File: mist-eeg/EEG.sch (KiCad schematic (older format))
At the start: 62 parts, among them J4 Electrodes, U11 ADS1299

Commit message: Hooked-up the SoM
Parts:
- renumbered TP10 to TP11
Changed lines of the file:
@@
 	1800 1500 1750 1500
 $Comp
-L power:GND #PWR089
+L power:GND #PWR088
 U 1 1 60A911F0
 P 1900 1600
-F 0 "#PWR089" H 1900 1350 50  0001 C CNN
+F 0 "#PWR088" H 1900 1350 50  0001 C CNN
 F 1 "GND" V 1905 1472 50  0000 R CNN
 F 2 "" H 1900 1600 50  0001 C CNN
@@
 	2100 3450 2200 3450
 $Comp
-L power:GND #PWR091
+L power:GND #PWR090
 U 1 1 60AB1BC7
 P 2100 3700
-F 0 "#PWR091" H 2100 3450 50  0001 C CNN
+F 0 "#PWR090" H 2100 3450 50  0001 C CNN
 F 1 "GND" H 2105 3527 50  0000 C CNN
 F 2 "" H 2100 3700 50  0001 C CNN
@@
 	9650 1400 9650 1350
 $Comp
-L Connector:TestPoint TP10
+L Connector:TestPoint TP11
 U 1 1 60AC454D
 P 9350 1200
-F 0 "TP10" H 9293 1318 50  0000 R CNN
+F 0 "TP11" H 9293 1318 50  0000 R CNN
 F 1 "VREFP" H 9293 1227 50  0000 R CNN
 F 2 "TestPoint:TestPoint_Pad_D1.0mm" H 9550 1200 50  0001 C CNN
@@
 	2000 6250 1950 6250
 $Comp
-L power:GND #PWR094
+L power:GND #PWR093
 U 1 1 60ACA9A2
 P 2300 6300
-F 0 "#PWR094" H 2300 6050 50  0001 C CNN
+F 0 "#PWR093" H 2300 6050 50  0001 C CNN
 F 1 "GND" V 2305 6172 50  0000 R CNN
 F 2 "" H 2300 6300 50  0001 C CNN
@@
 	2250 6250 2250 6150
 $Comp
-L power:GND #PWR085
+L power:GND #PWR084
 U 1 1 60AD4C0C
 P 1000 6700
-F 0 "#PWR085" H 1000 6450 50  0001 C CNN
+F 0 "#PWR084" H 1000 6450 50  0001 C CNN
 F 1 "GND" V 1005 6572 50  0000 R CNN
 F 2 "" H 1000 6700 50  0001 C CNN
@@
 	1000 6550 1050 6550
 $Comp
-L power:GND #PWR084
+L power:GND #PWR083
 U 1 1 60ADFB3C
 P 1000 6250
-F 0 "#PWR084" H 1000 6000 50  0001 C CNN
+F 0 "#PWR083" H 1000 6000 50  0001 C CNN
 F 1 "GND" V 1005 6122 50  0000 R CNN
 F 2 "" H 1000 6250 50  0001 C CNN
@@
 MOSI
 $Comp
-L power:GND #PWR087
+L power:GND #PWR086
 U 1 1 611E3BD9
 P 1350 4350
-F 0 "#PWR087" H 1350 4100 50  0001 C CNN
+F 0 "#PWR086" H 1350 4100 50  0001 C CNN
 F 1 "GND" H 1355 4177 50  0000 C CNN
 F 2 "" H 1350 4350 50  0001 C CNN
@@
 $EndComp
 $Comp
-L power:GND #PWR083
+L power:GND #PWR082
 U 1 1 611E3D9B
 P 850 2050
-F 0 "#PWR083" H 850 1800 50  0001 C CNN
+F 0 "#PWR082" H 850 1800 50  0001 C CNN
 F 1 "GND" H 855 1877 50  0000 C CNN
 F 2 "" H 850 2050 50  0001 C CNN
@@
 $EndComp
 $Comp
-L power:GND #PWR092
+L power:GND #PWR091
 U 1 1 611E4134
 P 2250 2450
-F 0 "#PWR092" H 2250 2200 50  0001 C CNN
+F 0 "#PWR091" H 2250 2200 50  0001 C CNN
 F 1 "GND" H 2255 2277 50  0000 C CNN
 F 2 "" H 2250 2450 50  0001 C CNN
@@
 $EndComp
 $Comp
-L power:GND #PWR0100
+L power:GND #PWR099
 U 1 1 611E45D1
 P 5950 5200
-F 0 "#PWR0100" H 5950 4950 50  0001 C CNN
+F 0 "#PWR099" H 5950 4950 50  0001 C CNN
 F 1 "GND" H 5955 5027 50  0000 C CNN
 F 2 "" H 5950 5200 50  0001 C CNN
@@
 $EndComp
 $Comp
-L power:GND #PWR0104
+L power:GND #PWR0103
 U 1 1 611E8589
 P 7700 5200
-F 0 "#PWR0104" H 7700 4950 50  0001 C CNN
+F 0 "#PWR0103" H 7700 4950 50  0001 C CNN
 F 1 "GND" H 7705 5027 50  0000 C CNN
 F 2 "" H 7700 5200 50  0001 C CNN
@@
 $EndComp
 $Comp
-L power:GND #PWR0103
+L power:GND #PWR0102
 U 1 1 611E895E
 P 7700 4200
-F 0 "#PWR0103" H 7700 3950 50  0001 C CNN
+F 0 "#PWR0102" H 7700 3950 50  0001 C CNN
 F 1 "GND" H 7705 4027 50  0000 C CNN
 F 2 "" H 7700 4200 50  0001 C CNN
@@
 $EndComp
 $Comp
-L power:GND #PWR0102
+L power:GND #PWR0101
 U 1 1 611E8B6C
 P 7700 3200
-F 0 "#PWR0102" H 7700 2950 50  0001 C CNN
+F 0 "#PWR0101" H 7700 2950 50  0001 C CNN
 F 1 "GND" H 7705 3027 50  0000 C CNN
 F 2 "" H 7700 3200 50  0001 C CNN
@@
 $EndComp
 $Comp
-L power:GND #PWR0101
+L power:GND #PWR0100
 U 1 1 611E8DAA
 P 7700 2150
-F 0 "#PWR0101" H 7700 1900 50  0001 C CNN
+F 0 "#PWR0100" H 7700 1900 50  0001 C CNN
 F 1 "GND" H 7705 1977 50  0000 C CNN
 F 2 "" H 7700 2150 50  0001 C CNN
@@
 $EndComp
 $Comp
-L power:GND #PWR097
+L power:GND #PWR096
 U 1 1 611E8FCE
 P 5950 2150
-F 0 "#PWR097" H 5950 1900 50  0001 C CNN
+F 0 "#PWR096" H 5950 1900 50  0001 C CNN
 F 1 "GND" H 5955 1977 50  0000 C CNN
 F 2 "" H 5950 2150 50  0001 C CNN
@@
 $EndComp
 $Comp
-L power:GND #PWR098
+L power:GND #PWR097
 U 1 1 611E9362
 P 5950 3200
-F 0 "#PWR098" H 5950 2950 50  0001 C CNN
+F 0 "#PWR097" H 5950 2950 50  0001 C CNN
 F 1 "GND" H 5955 3027 50  0000 C CNN
 F 2 "" H 5950 3200 50  0001 C CNN
@@
 $EndComp
 $Comp
-L power:GND #PWR099
+L power:GND #PWR098
 U 1 1 611E959E
 P 5950 4200
-F 0 "#PWR099" H 5950 3950 50  0001 C CNN
+F 0 "#PWR098" H 5950 3950 50  0001 C CNN
 F 1 "GND" H 5955 4027 50  0000 C CNN
 F 2 "" H 5950 4200 50  0001 C CNN
@@
 $EndComp
 $Comp
-L power:GND #PWR0106
+L power:GND #PWR0105
 U 1 1 611EC7A4
 P 9750 1450
-F 0 "#PWR0106" H 9750 1200 50  0001 C CNN
+F 0 "#PWR0105" H 9750 1200 50  0001 C CNN
 F 1 "GND" H 9755 1277 50  0000 C CNN
 F 2 "" H 9750 1450 50  0001 C CNN
@@
 $EndComp
 $Comp
-L power:GND #PWR0107
+L power:GND #PWR0106
 U 1 1 611EFAB9
 P 9900 6250
-F 0 "#PWR0107" H 9900 6000 50  0001 C CNN
+F 0 "#PWR0106" H 9900 6000 50  0001 C CNN
 F 1 "GND" H 9905 6077 50  0000 C CNN
 F 2 "" H 9900 6250 50  0001 C CNN
@@
 $EndComp
 $Comp
-L power:GND #PWR096
+L power:GND #PWR095
 U 1 1 611EFD90
 P 3950 5500
-F 0 "#PWR096" H 3950 5250 50  0001 C CNN
+F 0 "#PWR095" H 3950 5250 50  0001 C CNN
 F 1 "GND" H 3955 5327 50  0000 C CNN
 F 2 "" H 3950 5500 50  0001 C CNN
@@
 $EndComp
 $Comp
-L power:GND #PWR095
+L power:GND #PWR094
 U 1 1 611F02B8
 P 3950 4200
-F 0 "#PWR095" H 3950 3950 50  0001 C CNN
+F 0 "#PWR094" H 3950 3950 50  0001 C CNN
 F 1 "GND" H 3955 4027 50  0000 C CNN
 F 2 "" H 3950 4200 50  0001 C CNN
@@
 $EndComp
 $Comp
-L power:GND #PWR0105
+L power:GND #PWR0104
 U 1 1 611F35AF
 P 9350 4600
-F 0 "#PWR0105" H 9350 4350 50  0001 C CNN
+F 0 "#PWR0104" H 9350 4350 50  0001 C CNN
 F 1 "GND" H 9355 4427 50  0000 C CNN
 F 2 "" H 9350 4600 50  0001 C CNN
@@
 	1350 2700 1350 2800
 $Comp
-L power:GND #PWR086
+L power:GND #PWR085
 U 1 1 60DCA2D0
 P 1350 3050
-F 0 "#PWR086" H 1350 2800 50  0001 C CNN
+F 0 "#PWR085" H 1350 2800 50  0001 C CNN
 F 1 "GND" H 1355 2877 50  0000 C CNN
 F 2 "" H 1350 3050 50  0001 C CNN
@@
 Connection ~ 1350 3000
 $Comp
-L power:+3V3 #PWR088
+L power:+3V3 #PWR087
 U 1 1 6110D1DA
 P 1800 1450
-F 0 "#PWR088" H 1800 1300 50  0001 C CNN
+F 0 "#PWR087" H 1800 1300 50  0001 C CNN
 F 1 "+3V3" H 1815 1623 50  0000 C CNN
 F 2 "" H 1800 1450 50  0001 C CNN
@@
 $EndComp
 $Comp
-L power:+3V3 #PWR090
+L power:+3V3 #PWR089
 U 1 1 6110DA17
 P 2100 3350
-F 0 "#PWR090" H 2100 3200 50  0001 C CNN
+F 0 "#PWR089" H 2100 3200 50  0001 C CNN
 F 1 "+3V3" H 2115 3523 50  0000 C CNN
 F 2 "" H 2100 3350 50  0001 C CNN
@@
 $EndComp
 $Comp
-L power:+3V3 #PWR093
+L power:+3V3 #PWR092
 U 1 1 6110E217
 P 2250 6900
-F 0 "#PWR093" H 2250 6750 50  0001 C CNN
+F 0 "#PWR092" H 2250 6750 50  0001 C CNN
 F 1 "+3V3" V 2265 7028 50  0000 L CNN
 F 2 "" H 2250 6900 50  0001 C CNN

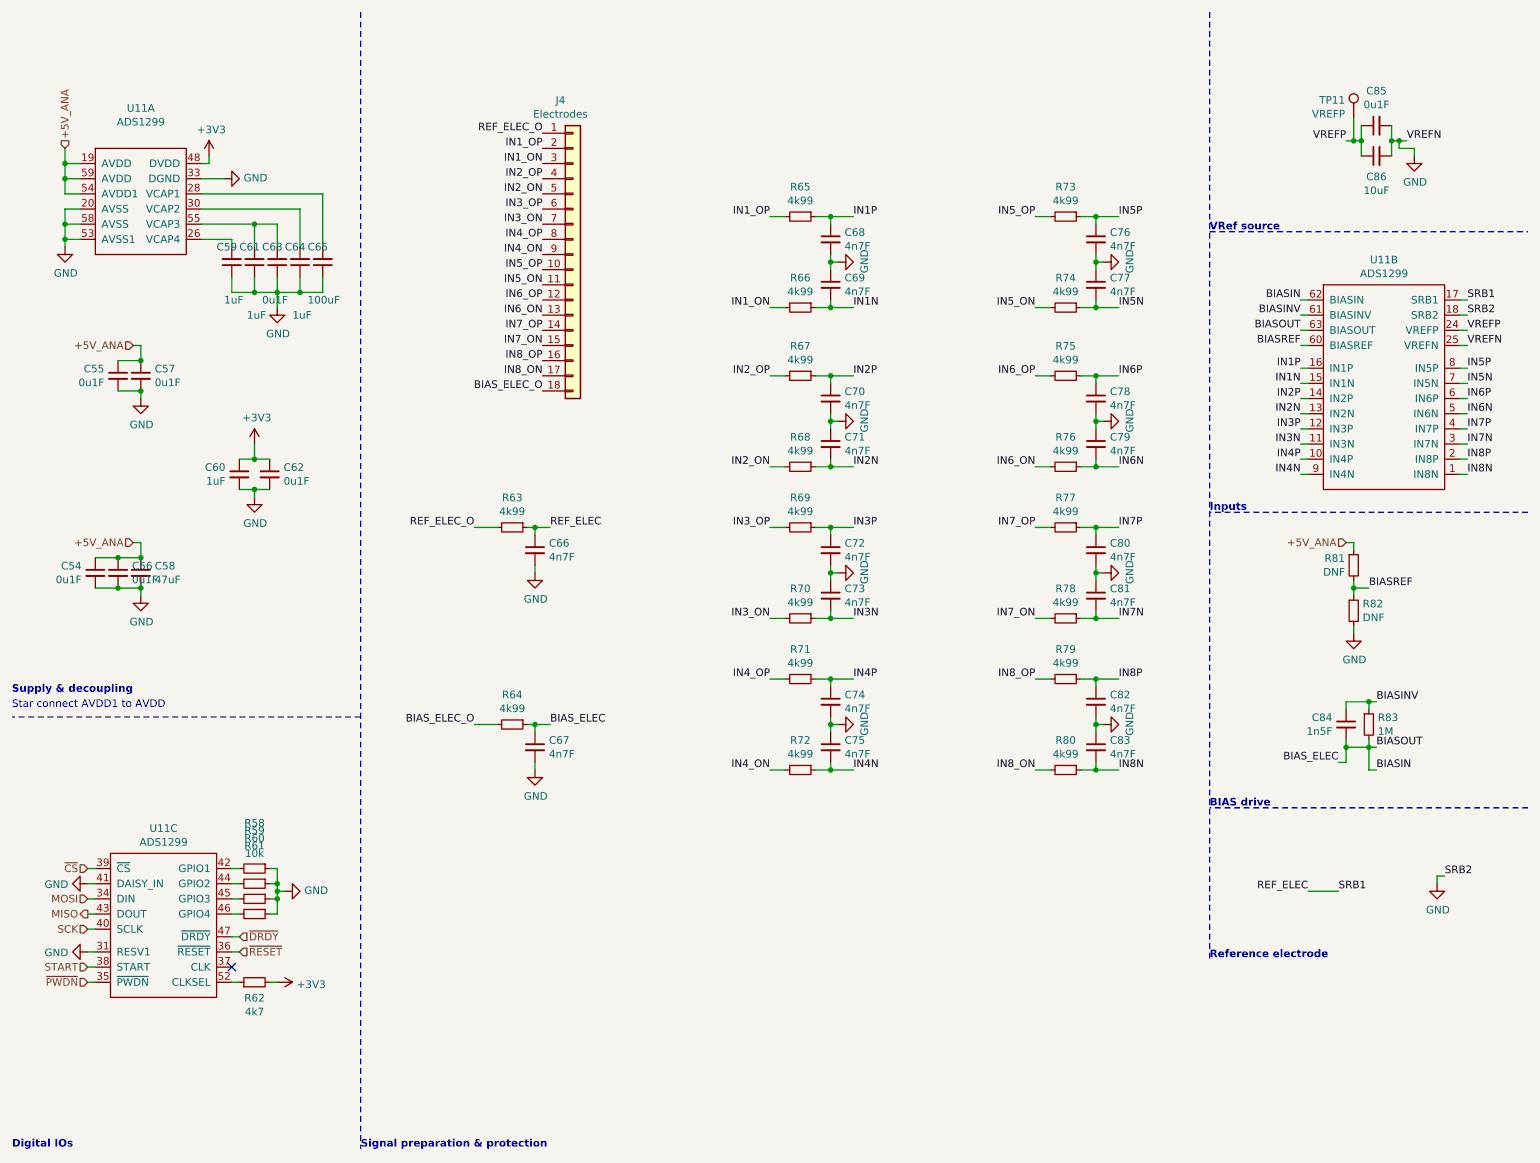
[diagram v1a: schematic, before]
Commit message: Finish schematic and create interface specifications
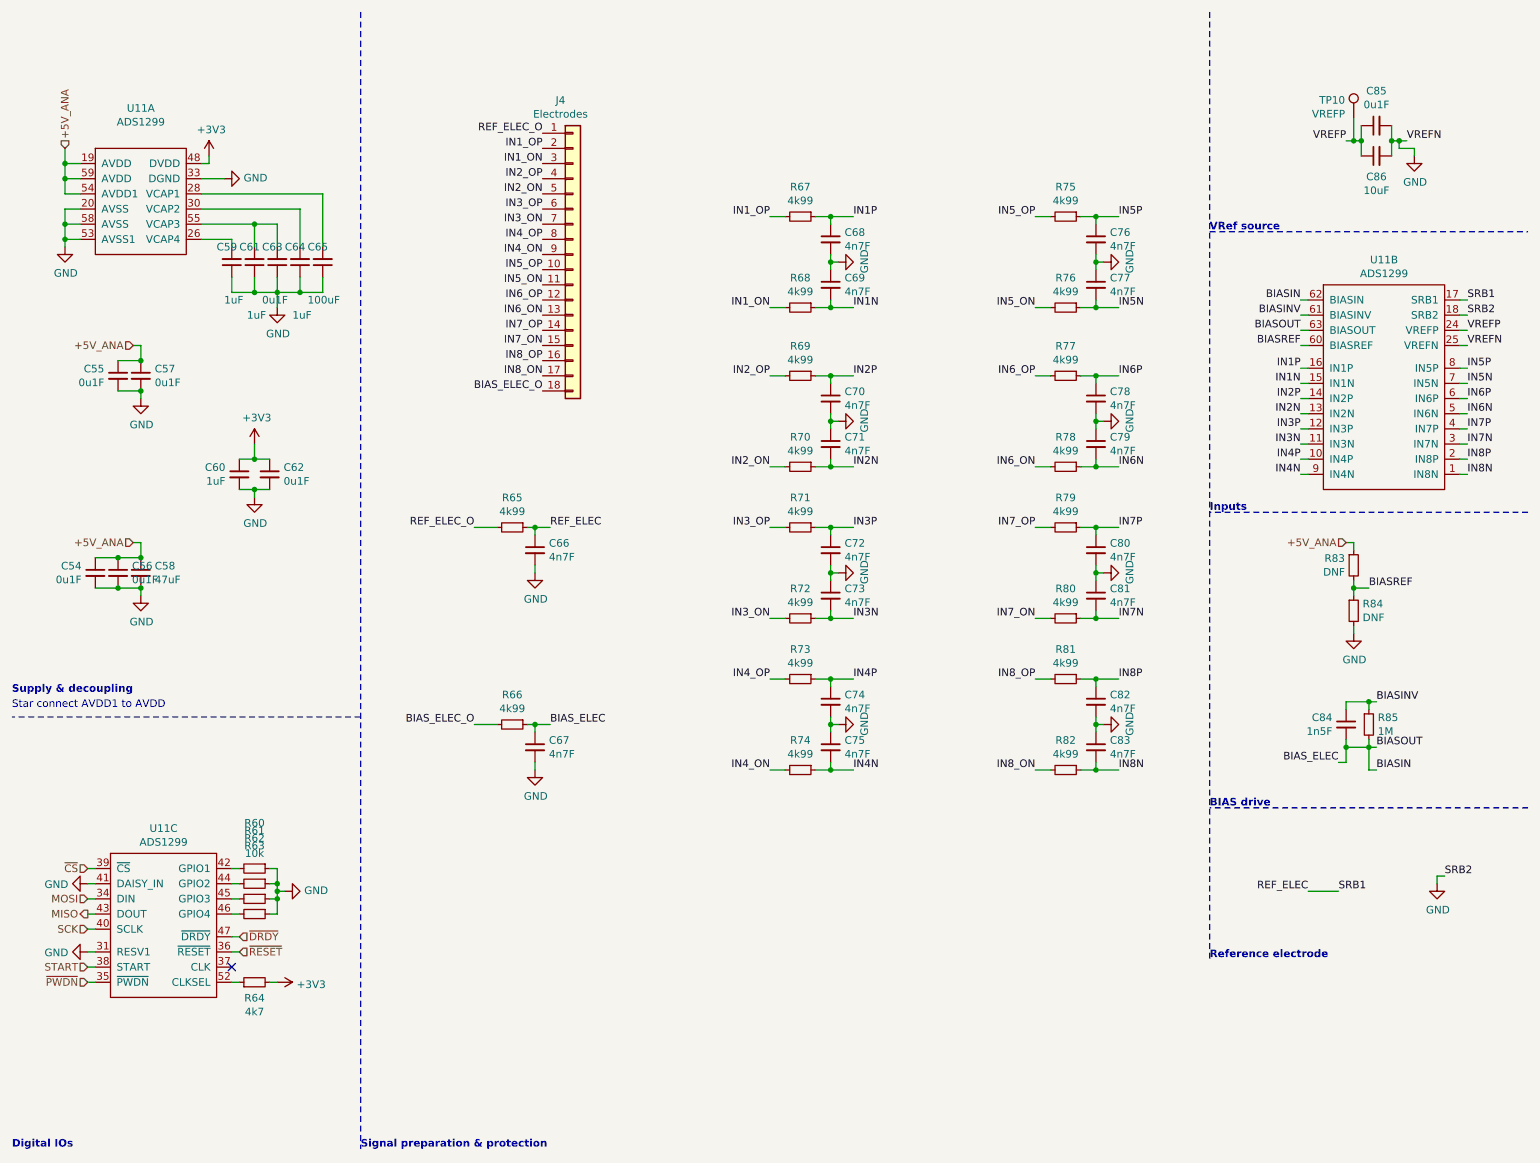
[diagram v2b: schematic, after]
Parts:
- renumbered R58 to R60, R59 to R61, R60 to R62, R61 to R63, R62 to R64, R63 to R65, R64 to R66, R65 to R67, R66 to R68, R67 to R69, R68 to R70, R69 to R71, R70 to R72, R71 to R73, R72 to R74, R73 to R75, R74 to R76, R75 to R77, R76 to R78, R77 to R79, R78 to R80, R79 to R81, R80 to R82, R81 to R83, R82 to R84, R83 to R85, TP11 to TP10

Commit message: Update footprints based upon piece availability & generate manufacturing files
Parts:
- C58, C65: footprint Capacitor_SMD:C_1206_3216Metric -> Capacitor_SMD:C_1210_3225Metric
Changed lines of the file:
@@
 F 0 "C58" H 1442 4246 50  0000 L CNN
 F 1 "47uF" H 1442 4155 50  0000 L CNN
-F 2 "Capacitor_SMD:C_1206_3216Metric" H 1350 4200 50  0001 C CNN
+F 2 "Capacitor_SMD:C_1210_3225Metric" H 1350 4200 50  0001 C CNN
 F 3 "~" H 1350 4200 50  0001 C CNN
 	1    1350 4200
@@
 F 0 "C65" H 2650 2050 50  0000 R CNN
 F 1 "100uF" H 2650 2400 50  0000 R CNN
-F 2 "Capacitor_SMD:C_1206_3216Metric" H 2550 2150 50  0001 C CNN
+F 2 "Capacitor_SMD:C_1210_3225Metric" H 2550 2150 50  0001 C CNN
 F 3 "~" H 2550 2150 50  0001 C CNN
 	1    2550 2150

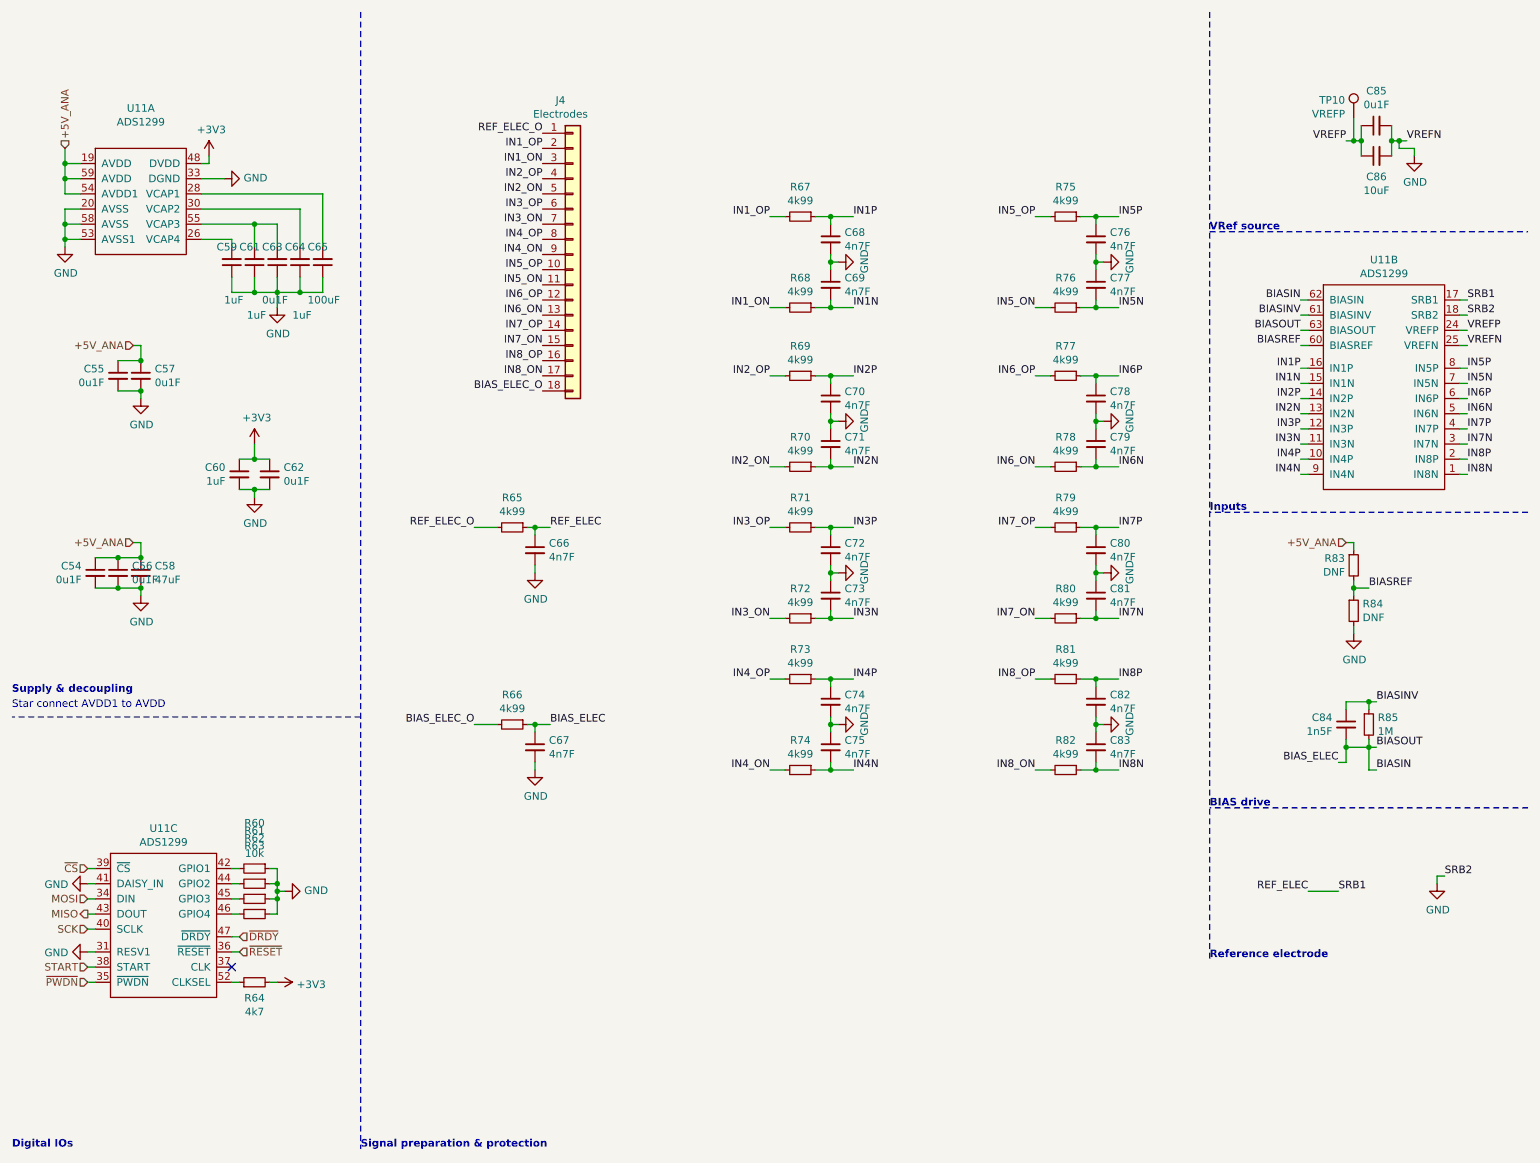
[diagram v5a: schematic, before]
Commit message: Change buckboost regulator used
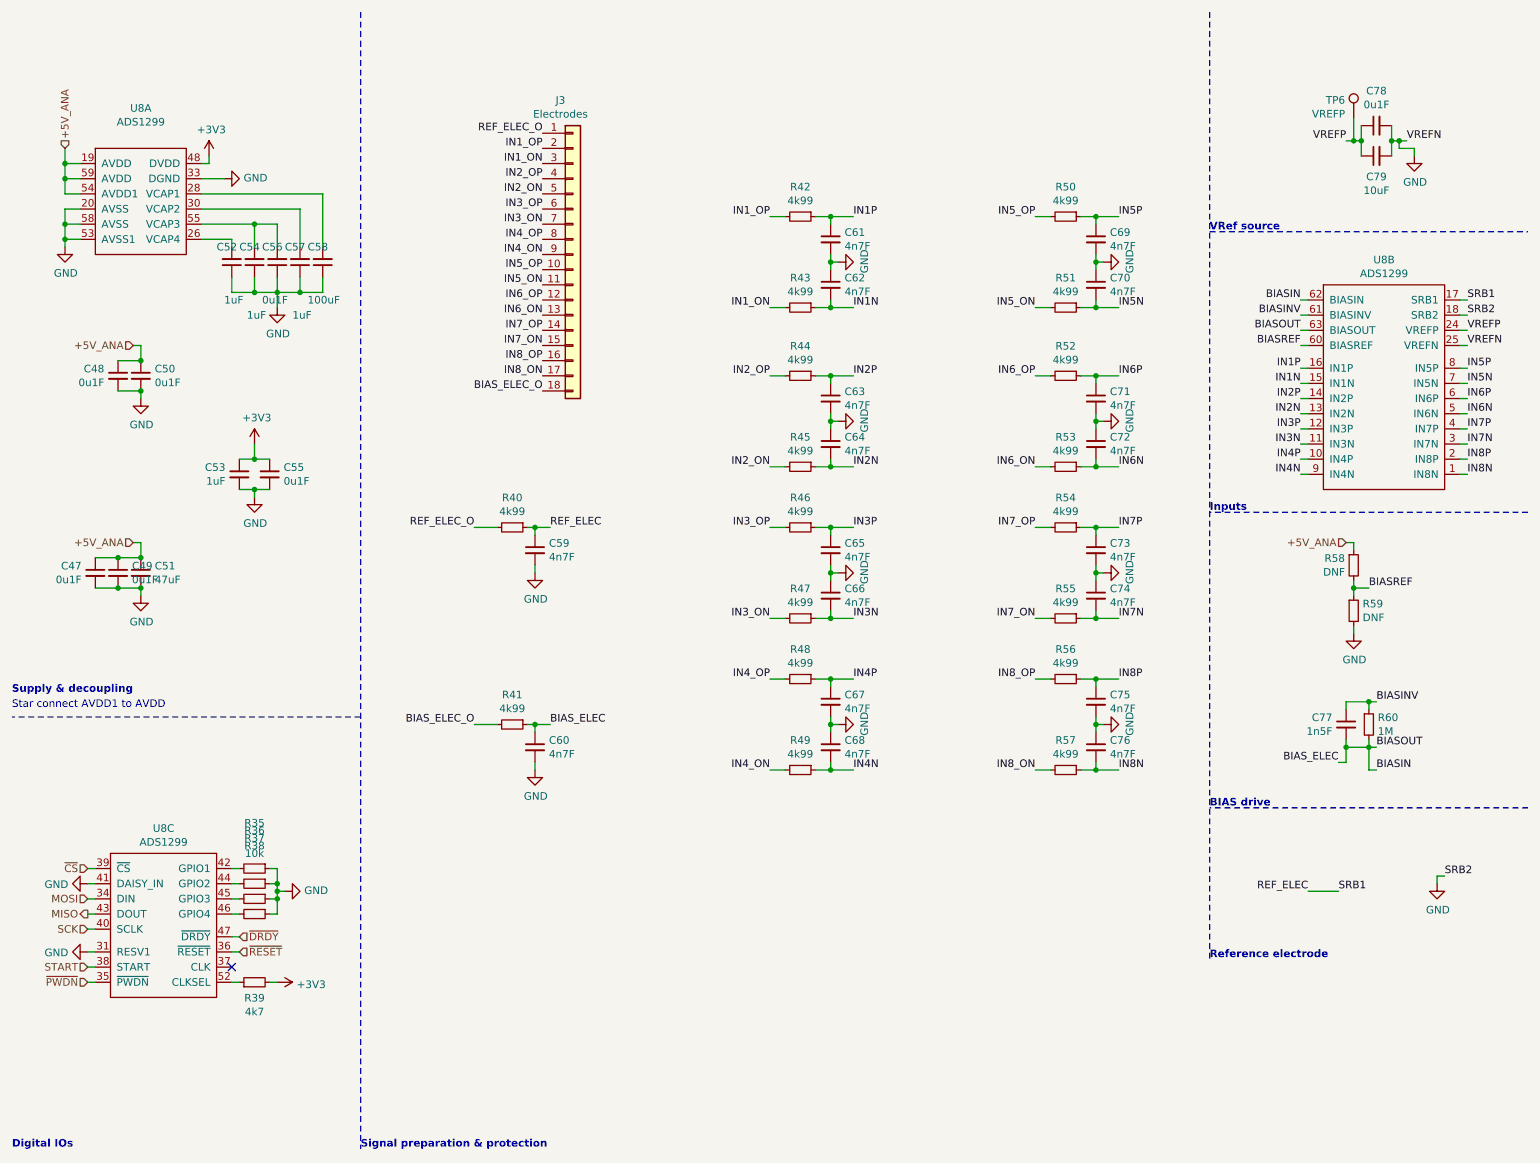
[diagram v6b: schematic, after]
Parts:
- renumbered C54 to C47, C55 to C48, C56 to C49, C57 to C50, C58 to C51, C59 to C52, C60 to C53, C61 to C54, C62 to C55, C63 to C56, C64 to C57, C65 to C58, C66 to C59, C67 to C60, C68 to C61, C69 to C62, C70 to C63, C71 to C64, C72 to C65, C73 to C66, C74 to C67, C75 to C68, C76 to C69, C77 to C70, C78 to C71, C79 to C72, C80 to C73, C81 to C74, C82 to C75, C83 to C76, C84 to C77, C85 to C78, C86 to C79, J4 to J3, R60 to R35, R61 to R36, R62 to R37, R63 to R38, R64 to R39, R65 to R40, R66 to R41, R67 to R42, R68 to R43, R69 to R44, R70 to R45, R71 to R46, R72 to R47, R73 to R48, R74 to R49, R75 to R50, R76 to R51, R77 to R52, R78 to R53, R79 to R54, R80 to R55, R81 to R56, R82 to R57, R83 to R58, R84 to R59, R85 to R60, TP10 to TP6, U11 to U8
